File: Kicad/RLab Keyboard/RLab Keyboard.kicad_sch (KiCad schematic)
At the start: 81 parts, among them J1 Conn_01x01_Pin, J10 Conn_01x01_Pin, J11 Conn_01x01_Pin, J12 Conn_01x01_Pin, J13 Conn_01x07, J14 Conn_01x09, J15 Conn_01x09, J16 Conn_01x09, J17 AudioJack3_Switch, J18 Conn_01x06, J19 Conn_01x06, J2 Conn_01x01_Pin, J20 Conn_01x06, J3 Conn_01x01_Pin, J4 Conn_01x01_Pin, J5 Conn_01x01_Pin, J6 Conn_01x01_Pin, J7 Conn_01x01_Pin, J8 Conn_01x01_Pin, J9 Conn_01x01_Pin, SW1 SW_MEC_5G, SW2 SW_MEC_5G, SW3 SW_MEC_5G, SW4 SW_MEC_5G, SW5 SW_MEC_5G, SW6 SW_MEC_5G, U1 LP5907MFX-3.3, U2 MPR121QR2, U3 74LVC1G17, U4 PCM5102, U5 LM386

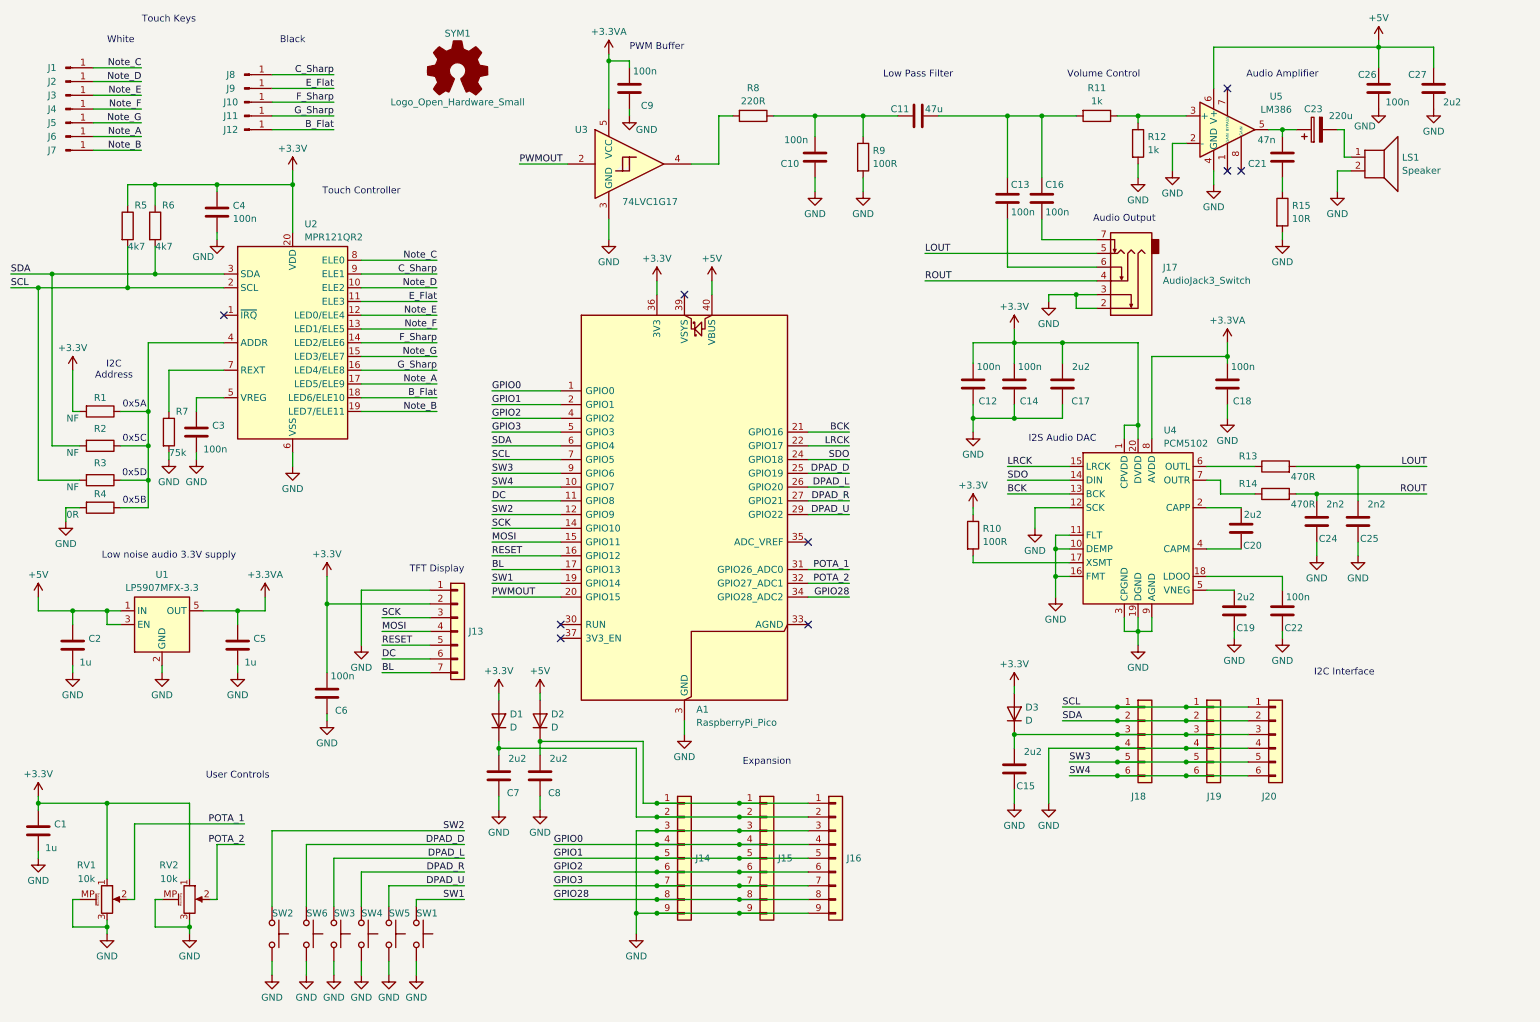
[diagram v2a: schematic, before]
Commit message: Files updated for JLCPCB Assembly
Added DNP  for through hole components. can be viewed as option in 3D viewer.
Production files in JLCPCB folder
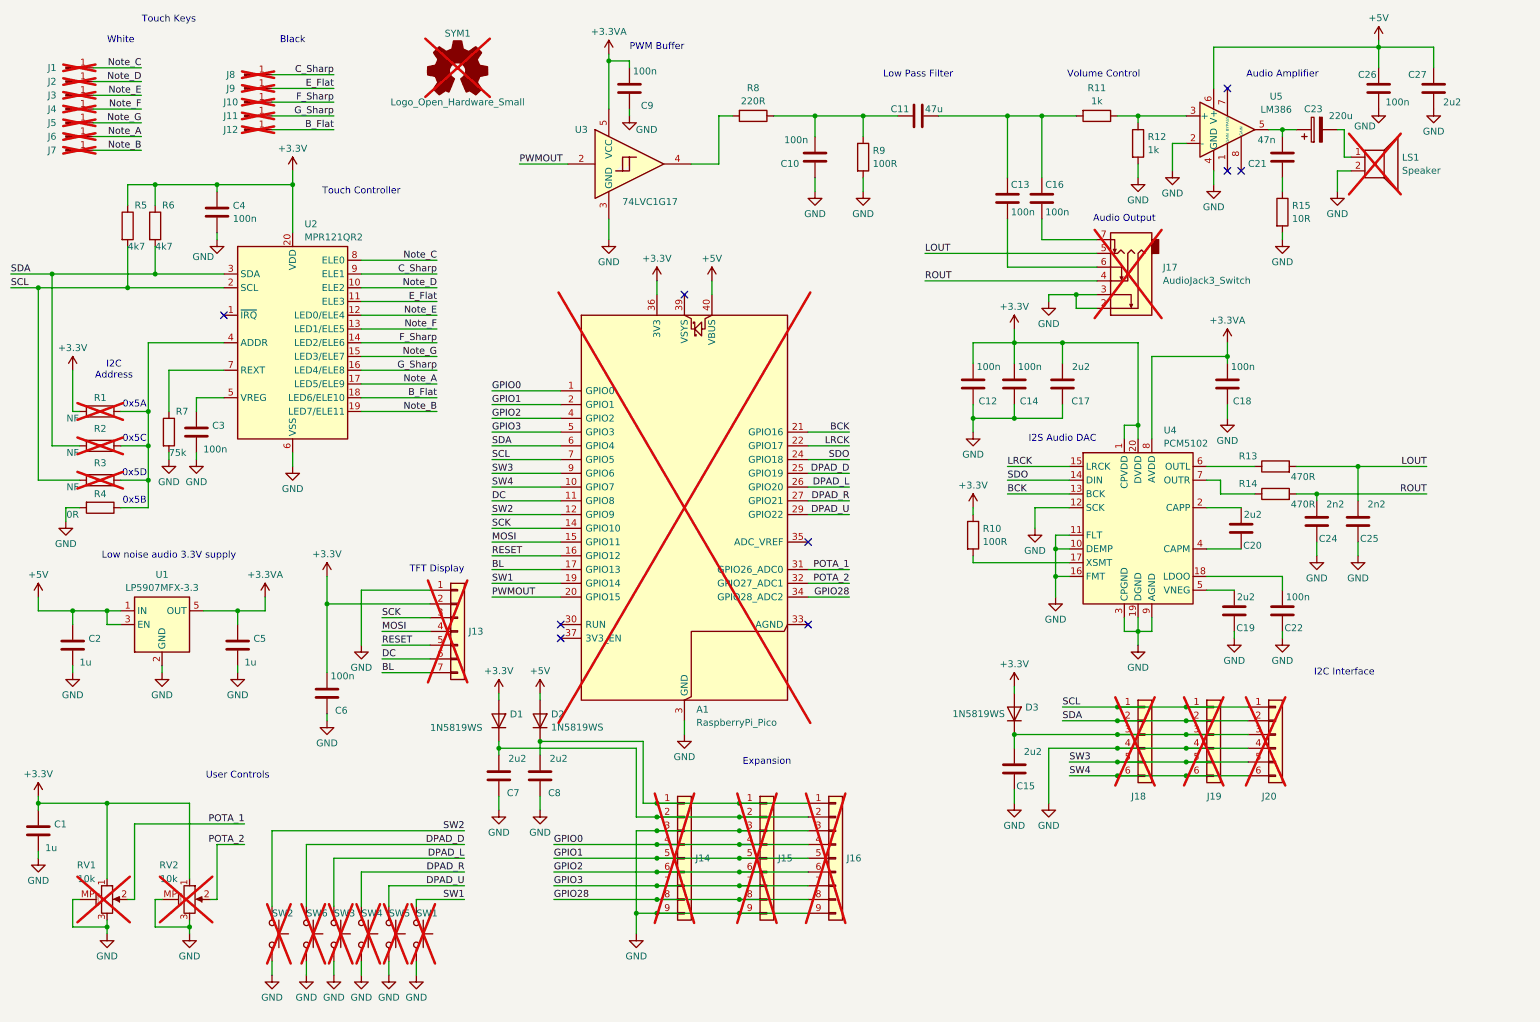
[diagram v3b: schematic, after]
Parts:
- A1, J1, J10, J11, J12, J13, J15, J16, J18, J2, J20, J3, J4, J5, J6, J7, J8, J9, LS1, R1, R2, R3, RV1, RV2, SW1, SW2, SW3, SW4, SW5, SW6: now not fitted
- C1, C2, C5: LCSC Part (none) -> C111590
- C10, C12, C13, C14, C16, C18, C22, C26, C3, C4, C6, C9: LCSC Part (none) -> C6119867
- C11: LCSC Part (none) -> C19103846
- C15, C17, C19, C20, C27, C7, C8: LCSC Part (none) -> C5189830
- C21: LCSC Part (none) -> C597218
- C23: LCSC Part (none) -> C412252
- C24, C25: LCSC Part (none) -> C1604
- D1, D2, D3: value D -> 1N5819WS; LCSC Part (none) -> C191023
- J14, J19, SYM1: now not fitted; now left out of the parts list
- J17: LCSC Part (none) -> C668606; now not fitted; now left out of the parts list
- R10, R9: LCSC Part (none) -> C105588
- R11, R12: LCSC Part (none) -> C22548
- R13, R14: LCSC Part (none) -> C114669
- R15: LCSC Part (none) -> C22859
- R4: LCSC Part (none) -> C95177
- R5, R6: LCSC Part (none) -> C99782
- R7: LCSC Part (none) -> C114636
- R8: LCSC Part (none) -> C107696
- U1: LCSC Part (none) -> C5370990
- U2: LCSC Part (none) -> C91322
- U3: LCSC Part (none) -> C19829654
- U4: LCSC Part (none) -> C107671
- U5: LCSC Part (none) -> C22438596
